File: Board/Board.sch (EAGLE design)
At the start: 106 parts, among them IC1 7805TV, IC2 LM358D, IC3 MCP23S17SO, IC4 ATMEGA328P_TQFP, IC5 MAX232SOIC16, IC6 MCP4921, IC7 TL431CD, IC8 DS18B20, IC9 DS18B20, Q1 IRF3710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

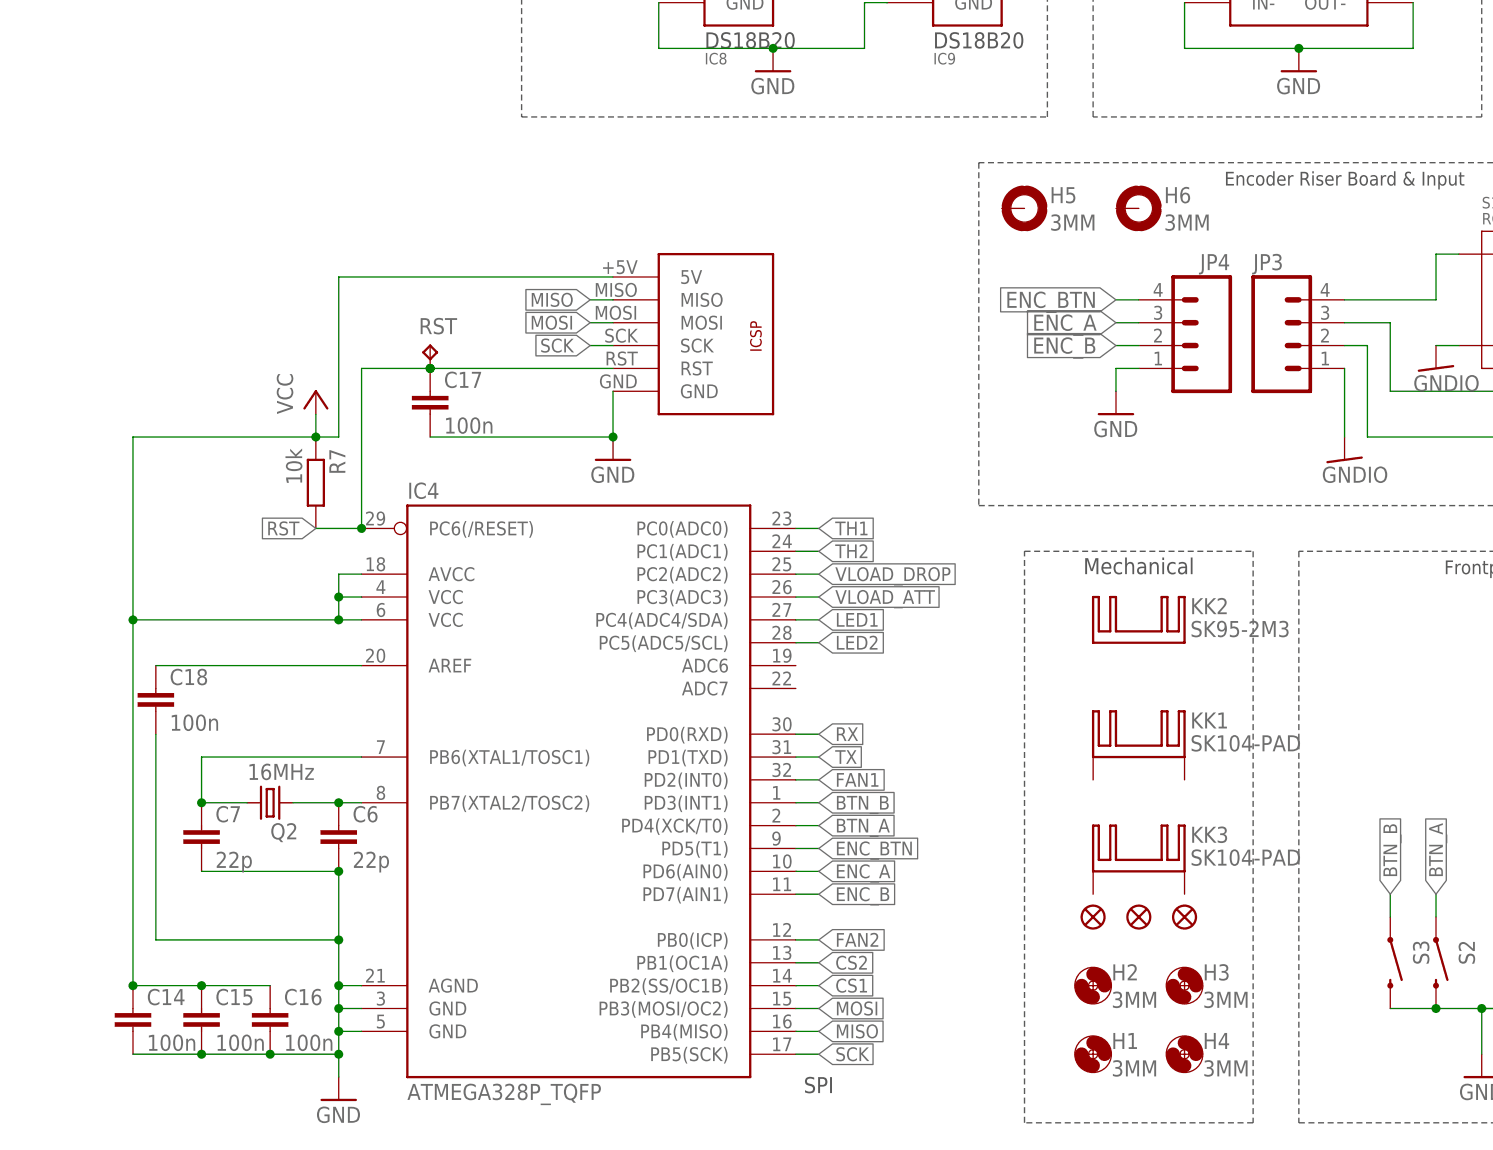
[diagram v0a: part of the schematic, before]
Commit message: renamed Board Files in preparation for Exporting PDFs
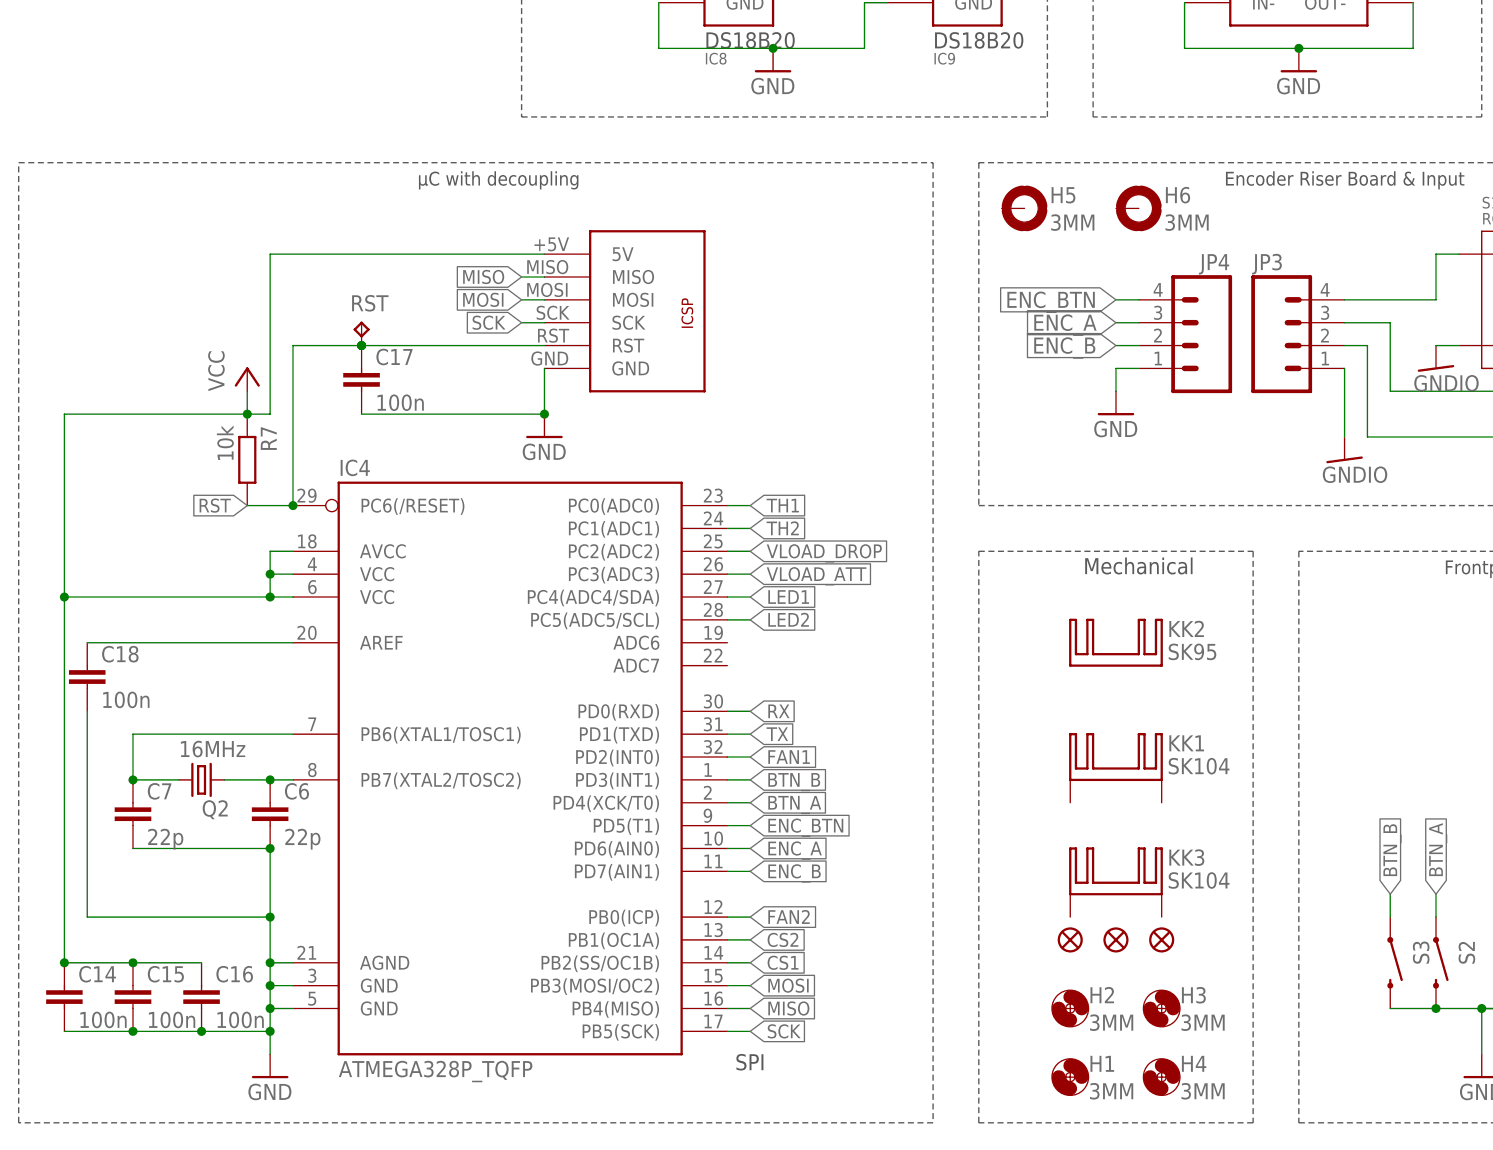
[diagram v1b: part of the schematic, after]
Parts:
- KK1, KK3: value SK104-PAD -> SK104
- KK2: value SK95-2M3 -> SK95
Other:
- note added: "µC with decoupling"
- moved on the sheet: C14, C15, C16, C17, C18, C6, C7, H1, H2, H3, H4, IC4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

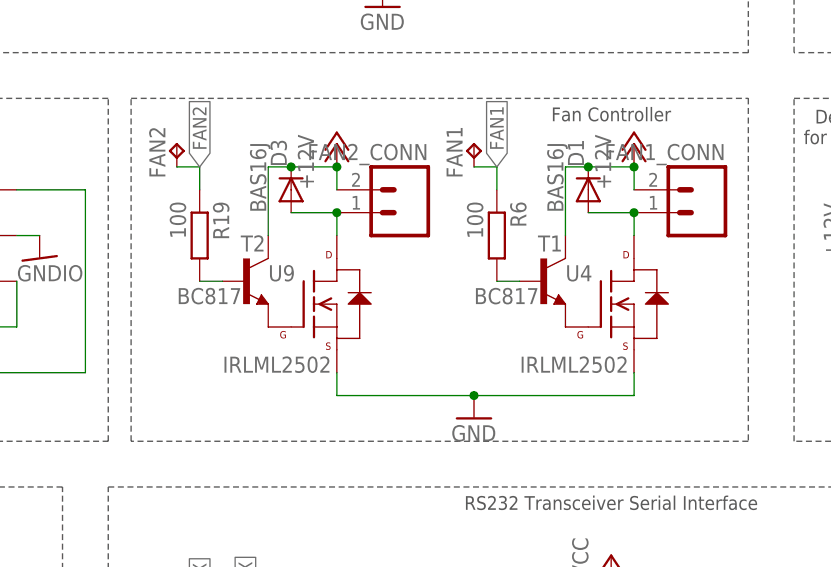
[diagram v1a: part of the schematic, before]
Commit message: added pull downs to fan drver gates
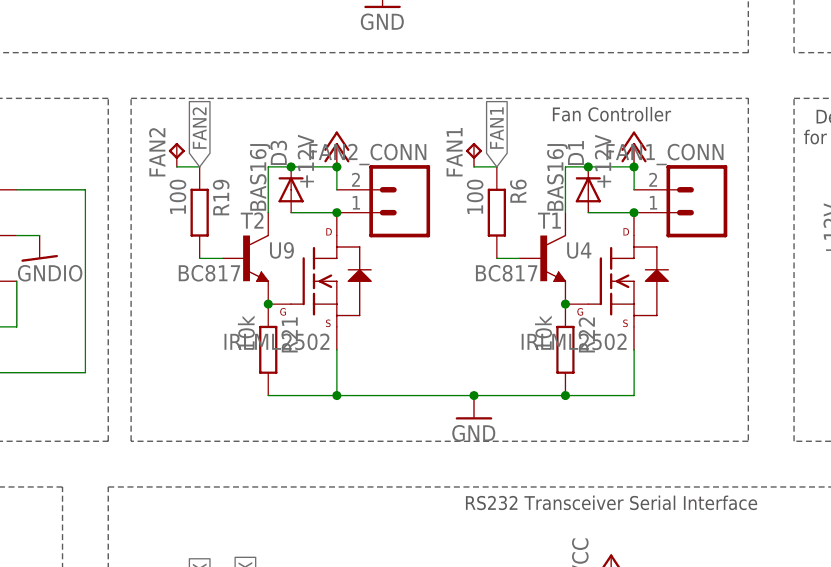
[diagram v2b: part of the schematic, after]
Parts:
- added R21, R22: 10k, rcl:R-EU_R1206
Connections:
- net GND: now also R21.2, R22.2
- net N$4: now also R22.1
- net N$42: now also R21.1
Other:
- moved on the sheet: R19, R6, T1, T2, U4, U9
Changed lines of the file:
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@@
 <part name="FID2" library="SparkFun-Aesthetics" deviceset="FIDUCIAL" device="1X2" value="FIDUCIAL1X2"/>
 <part name="FID3" library="SparkFun-Aesthetics" deviceset="FIDUCIAL" device="1X2" value="FIDUCIAL1X2"/>
+<part name="R21" library="rcl" deviceset="R-EU_" device="R1206" value="10k"/>
+<part name="R22" library="rcl" deviceset="R-EU_" device="R1206" value="10k"/>
 </parts>
 <sheets>
@@
 <instance part="H3" gate="G$1" x="-144.78" y="-88.9"/>
 <instance part="H4" gate="G$1" x="-144.78" y="-96.52"/>
-<instance part="U4" gate="G$1" x="-25.4" y="-17.78" smashed="yes">
-<attribute name="VALUE" x="-35.56" y="-25.4" size="1.778" layer="96"/>
-<attribute name="NAME" x="-30.48" y="-15.24" size="1.778" layer="95"/>
-</instance>
-<instance part="T1" gate="G$1" x="-33.02" y="-15.24" smashed="yes">
-<attribute name="NAME" x="-33.528" y="-11.938" size="1.778" layer="95"/>
-<attribute name="VALUE" x="-40.64" y="-17.78" size="1.778" layer="96"/>
+<instance part="U4" gate="G$1" x="-25.4" y="-15.24" smashed="yes">
+<attribute name="VALUE" x="-35.56" y="-22.86" size="1.778" layer="96"/>
+<attribute name="NAME" x="-30.48" y="-12.7" size="1.778" layer="95"/>
+</instance>
+<instance part="T1" gate="G$1" x="-33.02" y="-12.7" smashed="yes">
+<attribute name="NAME" x="-33.528" y="-9.398" size="1.778" layer="95"/>
+<attribute name="VALUE" x="-40.64" y="-15.24" size="1.778" layer="96"/>
 </instance>
 <instance part="P+7" gate="1" x="-22.86" y="0"/>
@@
 <attribute name="VALUE" x="-30.7086" y="-7.62" size="1.778" layer="96" rot="R90"/>
 </instance>
-<instance part="R6" gate="G$1" x="-38.1" y="-10.16" rot="R270"/>
+<instance part="R6" gate="G$1" x="-38.1" y="-7.62" rot="R270"/>
 <instance part="IC4" gate="U$1" x="-215.9" y="-63.5"/>
 <instance part="KK2" gate="G$1" x="-149.86" y="-50.8"/>
@@
 <attribute name="VALUE" x="-63.7286" y="-7.62" size="1.778" layer="96" rot="R90"/>
 </instance>
-<instance part="U9" gate="G$1" x="-58.42" y="-17.78" smashed="yes">
-<attribute name="VALUE" x="-68.58" y="-25.4" size="1.778" layer="96"/>
-<attribute name="NAME" x="-63.5" y="-15.24" size="1.778" layer="95"/>
-</instance>
-<instance part="T2" gate="G$1" x="-66.04" y="-15.24" smashed="yes">
-<attribute name="NAME" x="-66.548" y="-11.938" size="1.778" layer="95"/>
-<attribute name="VALUE" x="-73.66" y="-17.78" size="1.778" layer="96"/>
-</instance>
-<instance part="R19" gate="G$1" x="-71.12" y="-10.16" rot="R270"/>
+<instance part="U9" gate="G$1" x="-58.42" y="-15.24" smashed="yes">
+<attribute name="VALUE" x="-68.58" y="-22.86" size="1.778" layer="96"/>
+<attribute name="NAME" x="-63.5" y="-12.7" size="1.778" layer="95"/>
+</instance>
+<instance part="T2" gate="G$1" x="-66.04" y="-12.7" smashed="yes">
+<attribute name="NAME" x="-66.548" y="-9.398" size="1.778" layer="95"/>
+<attribute name="VALUE" x="-73.66" y="-15.24" size="1.778" layer="96"/>
+</instance>
+<instance part="R19" gate="G$1" x="-71.12" y="-7.62" rot="R270"/>
 <instance part="FAN2" gate="G$1" x="-73.66" y="0" smashed="yes">
 <attribute name="NAME" x="-74.93" y="-3.81" size="1.778" layer="95" rot="R90"/>
@@
 <instance part="FID2" gate="G$1" x="-144.78" y="-81.28"/>
 <instance part="FID3" gate="G$1" x="-149.86" y="-81.28"/>
+<instance part="R21" gate="G$1" x="-63.5" y="-22.86" rot="R270"/>
+<instance part="R22" gate="G$1" x="-30.48" y="-22.86" rot="R270"/>
 </instances>
 <busses>
@@
 <junction x="-22.86" y="-2.54"/>
 <pinref part="T1" gate="G$1" pin="C"/>
-<wire x1="-30.48" y1="-10.16" x2="-30.48" y2="-2.54" width="0.1524" layer="91"/>
+<wire x1="-30.48" y1="-7.62" x2="-30.48" y2="-2.54" width="0.1524" layer="91"/>
 <wire x1="-30.48" y1="-2.54" x2="-27.94" y2="-2.54" width="0.1524" layer="91"/>
 <junction x="-27.94" y="-2.54"/>
@@
 <junction x="-55.88" y="-2.54"/>
 <pinref part="T2" gate="G$1" pin="C"/>
-<wire x1="-63.5" y1="-10.16" x2="-63.5" y2="-2.54" width="0.1524" layer="91"/>
+<wire x1="-63.5" y1="-7.62" x2="-63.5" y2="-2.54" width="0.1524" layer="91"/>
 <wire x1="-63.5" y1="-2.54" x2="-60.96" y2="-2.54" width="0.1524" layer="91"/>
 <junction x="-60.96" y="-2.54"/>
@@
 <pinref part="U9" gate="G$1" pin="S"/>
 <wire x1="-40.64" y1="-27.94" x2="-55.88" y2="-27.94" width="0.1524" layer="91"/>
-<wire x1="-55.88" y1="-27.94" x2="-55.88" y2="-25.4" width="0.1524" layer="91"/>
+<wire x1="-55.88" y1="-27.94" x2="-55.88" y2="-22.86" width="0.1524" layer="91"/>
 <pinref part="U4" gate="G$1" pin="S"/>
-<wire x1="-40.64" y1="-27.94" x2="-22.86" y2="-27.94" width="0.1524" layer="91"/>
-<wire x1="-22.86" y1="-27.94" x2="-22.86" y2="-25.4" width="0.1524" layer="91"/>
+<wire x1="-40.64" y1="-27.94" x2="-30.48" y2="-27.94" width="0.1524" layer="91"/>
+<wire x1="-30.48" y1="-27.94" x2="-22.86" y2="-27.94" width="0.1524" layer="91"/>
+<wire x1="-22.86" y1="-27.94" x2="-22.86" y2="-22.86" width="0.1524" layer="91"/>
 <junction x="-40.64" y="-27.94"/>
+<pinref part="R21" gate="G$1" pin="2"/>
+<wire x1="-63.5" y1="-27.94" x2="-55.88" y2="-27.94" width="0.1524" layer="91"/>
+<junction x="-55.88" y="-27.94"/>
+<pinref part="R22" gate="G$1" pin="2"/>
+<junction x="-30.48" y="-27.94"/>
 </segment>
 <segment>
@@
 <pinref part="T1" gate="G$1" pin="E"/>
 <pinref part="U4" gate="G$1" pin="G"/>
+<pinref part="R22" gate="G$1" pin="1"/>
+<pinref part="R22" gate="G$1" pin="1"/>
+<junction x="-30.48" y="-17.78"/>
 </segment>
 </net>
@@
 <segment>
 <pinref part="U4" gate="G$1" pin="D"/>
-<wire x1="-22.86" y1="-10.16" x2="-22.86" y2="-7.62" width="0.1524" layer="91"/>
 <pinref part="D1" gate="G$1" pin="A"/>
 <wire x1="-22.86" y1="-7.62" x2="-27.94" y2="-7.62" width="0.1524" layer="91"/>
@@
 <pinref part="T1" gate="G$1" pin="B"/>
 <pinref part="R6" gate="G$1" pin="2"/>
-<wire x1="-38.1" y1="-15.24" x2="-35.56" y2="-15.24" width="0.1524" layer="91"/>
+<wire x1="-38.1" y1="-12.7" x2="-35.56" y2="-12.7" width="0.1524" layer="91"/>
 </segment>
 </net>
@@
 <pinref part="U9" gate="G$1" pin="G"/>
 <pinref part="T2" gate="G$1" pin="E"/>
+<pinref part="R21" gate="G$1" pin="1"/>
+<pinref part="R21" gate="G$1" pin="1"/>
+<junction x="-63.5" y="-17.78"/>
 </segment>
 </net>
@@
 <pinref part="T2" gate="G$1" pin="B"/>
 <pinref part="R19" gate="G$1" pin="2"/>
-<wire x1="-68.58" y1="-15.24" x2="-71.12" y2="-15.24" width="0.1524" layer="91"/>
+<wire x1="-68.58" y1="-12.7" x2="-71.12" y2="-12.7" width="0.1524" layer="91"/>
 </segment>
 </net>
@@
 <wire x1="-60.96" y1="-7.62" x2="-55.88" y2="-7.62" width="0.1524" layer="91"/>
 <pinref part="U9" gate="G$1" pin="D"/>
-<wire x1="-55.88" y1="-7.62" x2="-55.88" y2="-10.16" width="0.1524" layer="91"/>
 <junction x="-55.88" y="-7.62"/>
 </segment>
@@
 <segment>
 <pinref part="R19" gate="G$1" pin="1"/>
-<wire x1="-71.12" y1="-5.08" x2="-71.12" y2="-2.54" width="0.1524" layer="91"/>
 <pinref part="FAN2" gate="G$1" pin="TP"/>
 <wire x1="-73.66" y1="-2.54" x2="-71.12" y2="-2.54" width="0.1524" layer="91"/>
@@
 <segment>
 <pinref part="R6" gate="G$1" pin="1"/>
-<wire x1="-38.1" y1="-5.08" x2="-38.1" y2="-2.54" width="0.1524" layer="91"/>
 <label x="-38.1" y="-2.54" size="1.524" layer="95" rot="R90" xref="yes"/>
 <pinref part="FAN1" gate="G$1" pin="TP"/>

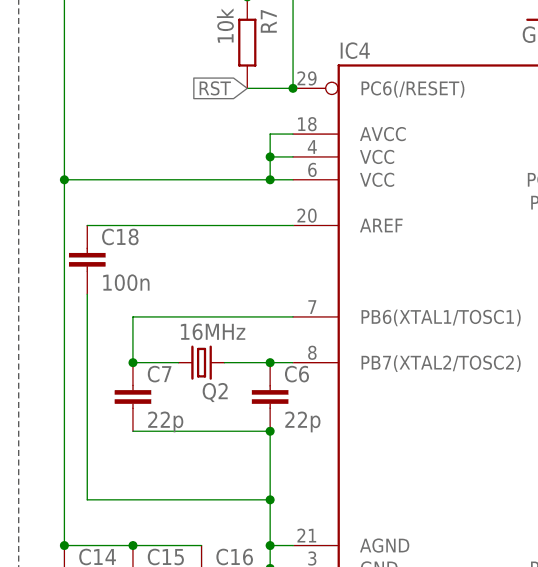
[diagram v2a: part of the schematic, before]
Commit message: lowered decoupling capacitance for VREF to allow fast switching of references
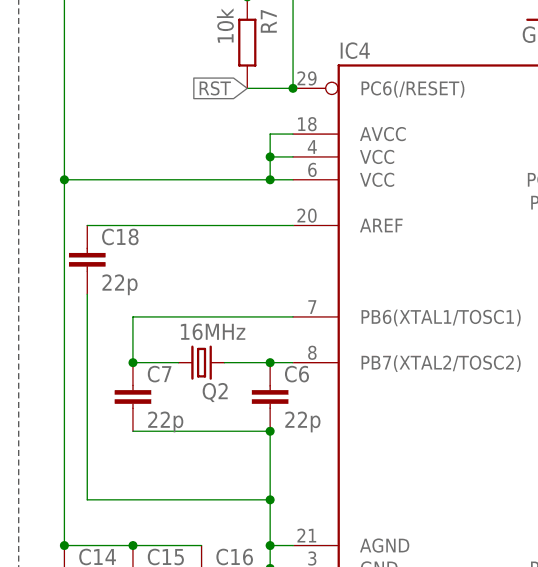
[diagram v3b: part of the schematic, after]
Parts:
- C18: value 100n -> 22p
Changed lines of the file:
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@@
 <part name="R12" library="rcl" deviceset="R-EU_" device="R1206" value="10k"/>
 <part name="R13" library="rcl" deviceset="R-EU_" device="R1206" value="3k"/>
-<part name="C18" library="rcl" deviceset="C-EU" device="C1206K" value="100n"/>
+<part name="C18" library="rcl" deviceset="C-EU" device="C1206K" value="22p"/>
 <part name="GND10" library="supply1" deviceset="GND" device=""/>
 <part name="VLOAD_ATT" library="testpad" deviceset="TP" device="B1,27"/>
